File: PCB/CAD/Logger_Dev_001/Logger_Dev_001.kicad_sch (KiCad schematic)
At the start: 11 parts, among them U2 ESP32-C6-WROOM-1

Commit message: Schematic finalised
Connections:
- no-connect marks 0 -> 11
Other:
- removed sheet Real Time Clock Module
- moved on the sheet: C10, C11, C12, C13, C6, R15, R16, S1, S2, S3, U2

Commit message: Update some footprints
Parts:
- U2: footprint PCM_Espressif:ESP32-C6-WROOM-1 -> ESPRESSIF footprints:ESP32-C6-WROOM-1
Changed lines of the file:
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@@
 			)
 		)
-		(property "Footprint" "PCM_Espressif:ESP32-C6-WROOM-1"
+		(property "Footprint" "ESPRESSIF footprints:ESP32-C6-WROOM-1"
 			(at 97.79 172.085 0)
 			(effects

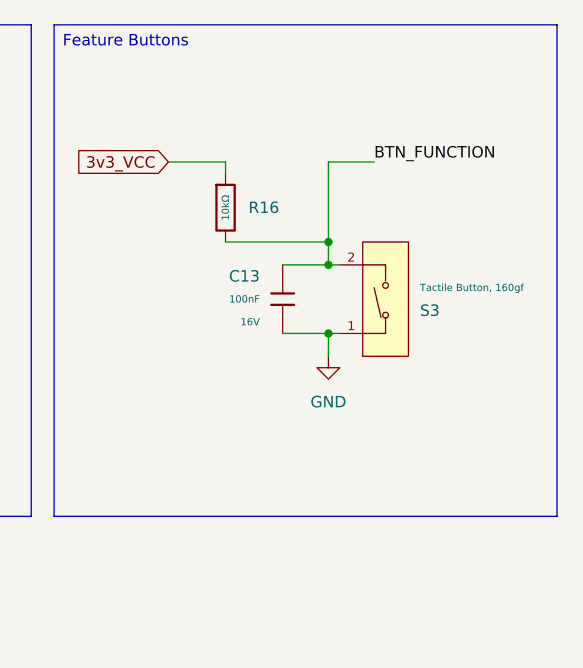
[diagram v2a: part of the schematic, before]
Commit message: PCB Layout Update
PCB Board Fixed
Most Components except Resistors placed
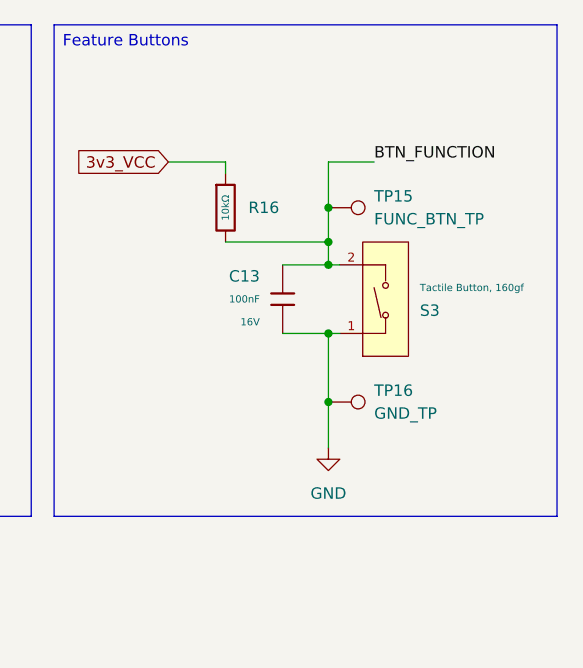
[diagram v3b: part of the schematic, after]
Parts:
- added TP15: FUNC_BTN_TP, TestPoint:TestPoint_Pad_D2.5mm, symbol Connector:TestPoint
- added TP16: GND_TP, TestPoint:TestPoint_Pad_D2.5mm, symbol Connector:TestPoint
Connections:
- net BTN_FUNCTION: now also TP15.1
- net GND: now also TP16.1
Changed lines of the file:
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@@
+	)
+	(junction
+		(at 254 121.92)
+		(diameter 0)
+		(color 0 0 0 0)
 	)
 	(junction
@@
 	)
 	(junction
+		(at 254 143.51)
+		(diameter 0)
+		(color 0 0 0 0)
+	)
+	(junction
 		(at 48.26 99.06)
 		(diameter 0)
@@
 	(wire
 		(pts
+			(xy 254 121.92) (xy 254 125.73)
+		)
+		(stroke
+			(width 0)
+			(type default)
+		)
+	)
+	(wire
+		(pts
 			(xy 125.73 127) (xy 128.27 127)
 		)
@@
 	(wire
 		(pts
+			(xy 254 143.51) (xy 254 135.89)
+		)
+		(stroke
+			(width 0)
+			(type default)
+		)
+	)
+	(wire
+		(pts
 			(xy 67.31 106.68) (xy 69.85 106.68)
 		)
@@
 	(wire
 		(pts
-			(xy 254 116.84) (xy 254 125.73)
+			(xy 254 116.84) (xy 254 121.92)
 		)
 		(stroke
@@
 	(wire
 		(pts
-			(xy 254 138.43) (xy 254 135.89)
+			(xy 254 148.59) (xy 254 143.51)
 		)
 		(stroke
@@
 	)
 	(symbol
+		(lib_id "Connector:TestPoint")
+		(at 254 121.92 270)
+		(unit 1)
+		(exclude_from_sim no)
+		(in_bom yes)
+		(on_board yes)
+		(dnp no)
+		(fields_autoplaced yes)
+		(property "Reference" "TP15"
+			(at 259.08 120.6499 90)
+			(effects
+				(font
+					(size 1.27 1.27)
+				)
+				(justify left)
+			)
+		)
+		(property "Value" "FUNC_BTN_TP"
+			(at 259.08 123.1899 90)
+			(effects
+				(font
+					(size 1.27 1.27)
+				)
+				(justify left)
+			)
+		)
+		(property "Footprint" "TestPoint:TestPoint_Pad_D2.5mm"
+			(at 254 127 0)
+			(effects
+				(font
+					(size 1.27 1.27)
+				)
+				(hide yes)
+			)
+		)
+		(property "Datasheet" "~"
+			(at 254 127 0)
+			(effects
+				(font
+					(size 1.27 1.27)
+				)
+				(hide yes)
+			)
+		)
+		(property "Description" "test point"
+			(at 254 121.92 0)
+			(effects
+				(font
+					(size 1.27 1.27)
+				)
+				(hide yes)
+			)
+		)
+		(pin "1"
+		)
+		(instances
+			(project "Logger_Dev_001"
+				(path "/9546b831-c7ee-4f40-8993-5fd5a38d4078"
+					(reference "TP15")
+					(unit 1)
+				)
+			)
+		)
+	)
+	(symbol
 		(lib_id "PCM_JLCPCB-Capacitors:0402,100nF")
 		(at 248.92 132.08 0)
@@
 	(symbol
 		(lib_id "power:GND")
-		(at 254 138.43 0)
+		(at 254 148.59 0)
 		(unit 1)
 		(exclude_from_sim no)
@@
 		(fields_autoplaced yes)
 		(property "Reference" "#PWR021"
-			(at 254 144.78 0)
+			(at 254 154.94 0)
 			(effects
 				(font
@@
 		)
 		(property "Value" "GND"
-			(at 254 143.51 0)
+			(at 254 153.67 0)
 			(effects
 				(font
@@
 		)
 		(property "Footprint" ""
-			(at 254 138.43 0)
+			(at 254 148.59 0)
 			(effects
 				(font
@@
 		)
 		(property "Datasheet" ""
-			(at 254 138.43 0)
+			(at 254 148.59 0)
 			(effects
 				(font
@@
 		)
 		(property "Description" "Power symbol creates a global label with name \"GND\" , ground"
-			(at 254 138.43 0)
+			(at 254 148.59 0)
 			(effects
 				(font
@@
 					(unit 1)
 				)
+			)
+		)
+	)
+	(symbol
+		(lib_id "Connector:TestPoint")
+		(at 254 143.51 270)
+		(unit 1)
+		(exclude_from_sim no)
+		(in_bom yes)
+		(on_board yes)
+		(dnp no)
+		(fields_autoplaced yes)
+		(property "Reference" "TP16"
+			(at 259.08 142.2399 90)
+			(effects
+				(font
+					(size 1.27 1.27)
+				)
+				(justify left)
+			)
+		)
+		(property "Value" "GND_TP"
+			(at 259.08 144.7799 90)
+			(effects
+				(font
+					(size 1.27 1.27)
+				)
+				(justify left)
+			)
+		)
+		(property "Footprint" "TestPoint:TestPoint_Pad_D2.5mm"
+			(at 254 148.59 0)
+			(effects
+				(font
+					(size 1.27 1.27)
+				)
+				(hide yes)
+			)
+		)
+		(property "Datasheet" "~"
+			(at 254 148.59 0)
+			(effects
+				(font
+					(size 1.27 1.27)
+				)
+				(hide yes)
+			)
+		)
+		(property "Description" "test point"
+			(at 254 143.51 0)
+			(effects
+				(font
+					(size 1.27 1.27)
+				)
+				(hide yes)
+			)
+		)
+		(pin "1"
+		)
+		(instances
+			(project "Logger_Dev_001"
+				(path "/9546b831-c7ee-4f40-8993-5fd5a38d4078"
+					(reference "TP16")
+					(unit 1)
+				)

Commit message: Update via size to reduce cost
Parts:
- TP15, TP16: now left out of the parts list
- U2: LCSC (none) -> C5366877
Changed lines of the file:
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@@
 		(unit 1)
 		(exclude_from_sim no)
-		(in_bom yes)
+		(in_bom no)
 		(on_board yes)
 		(dnp no)
@@
 			)
 		)
+		(property "LCSC" "C5366877"
+			(at 97.79 127 0)
+			(effects
+				(font
+					(size 1.27 1.27)
+				)
+				(hide yes)
+			)
+		)
 		(pin "6"
 		)
@@
 		(unit 1)
 		(exclude_from_sim no)
-		(in_bom yes)
+		(in_bom no)
 		(on_board yes)
 		(dnp no)
